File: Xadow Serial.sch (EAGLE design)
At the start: 29 parts, among them J1 CONNECTOR-HEADER-8P-3461050P1, J2 12p 0.5mm bottom contact, J3 12p 0.5mm bottom contact, J4 12p 0.5mm bottom contact, SW2 ADDR, U1 SC16IS750, U2 BSS138PS, X1 CTS_32X25_SMD

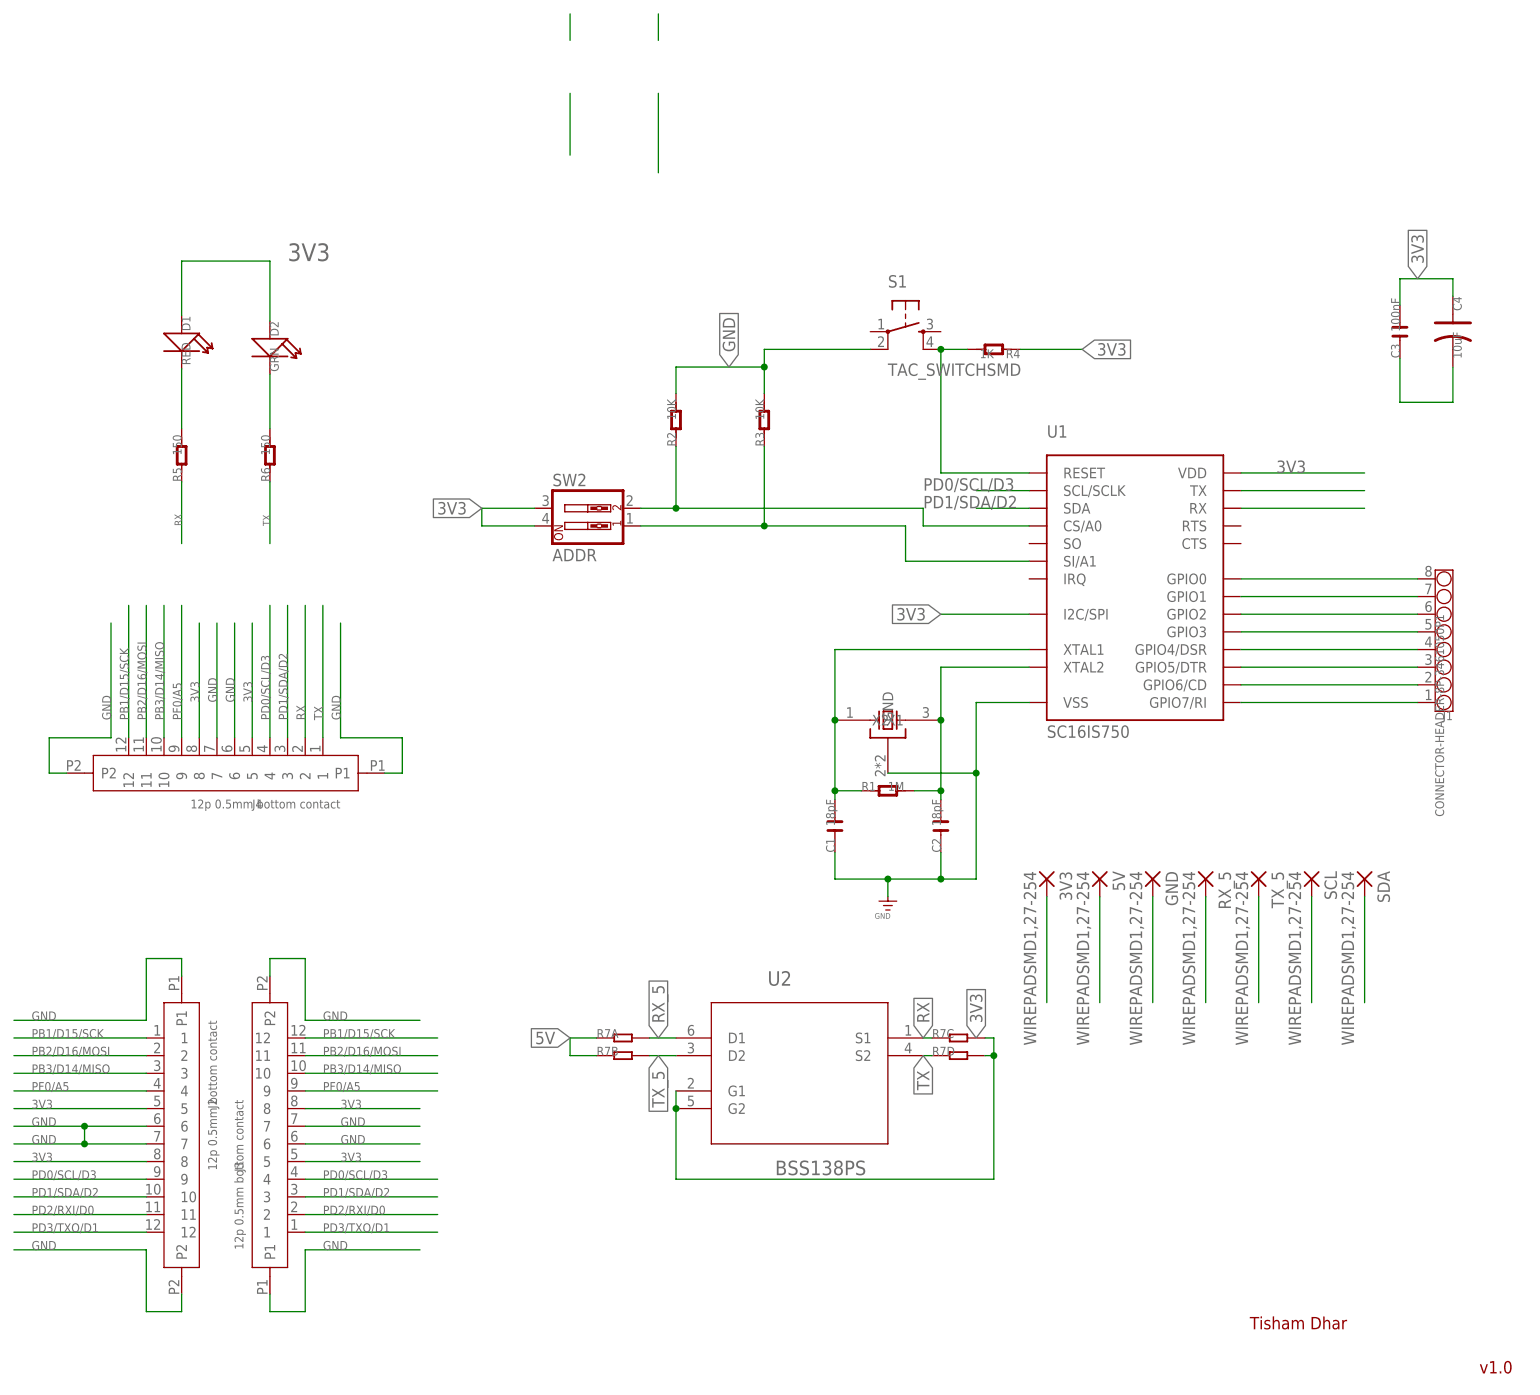
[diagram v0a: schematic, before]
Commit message: Fully routed with solder jumpers
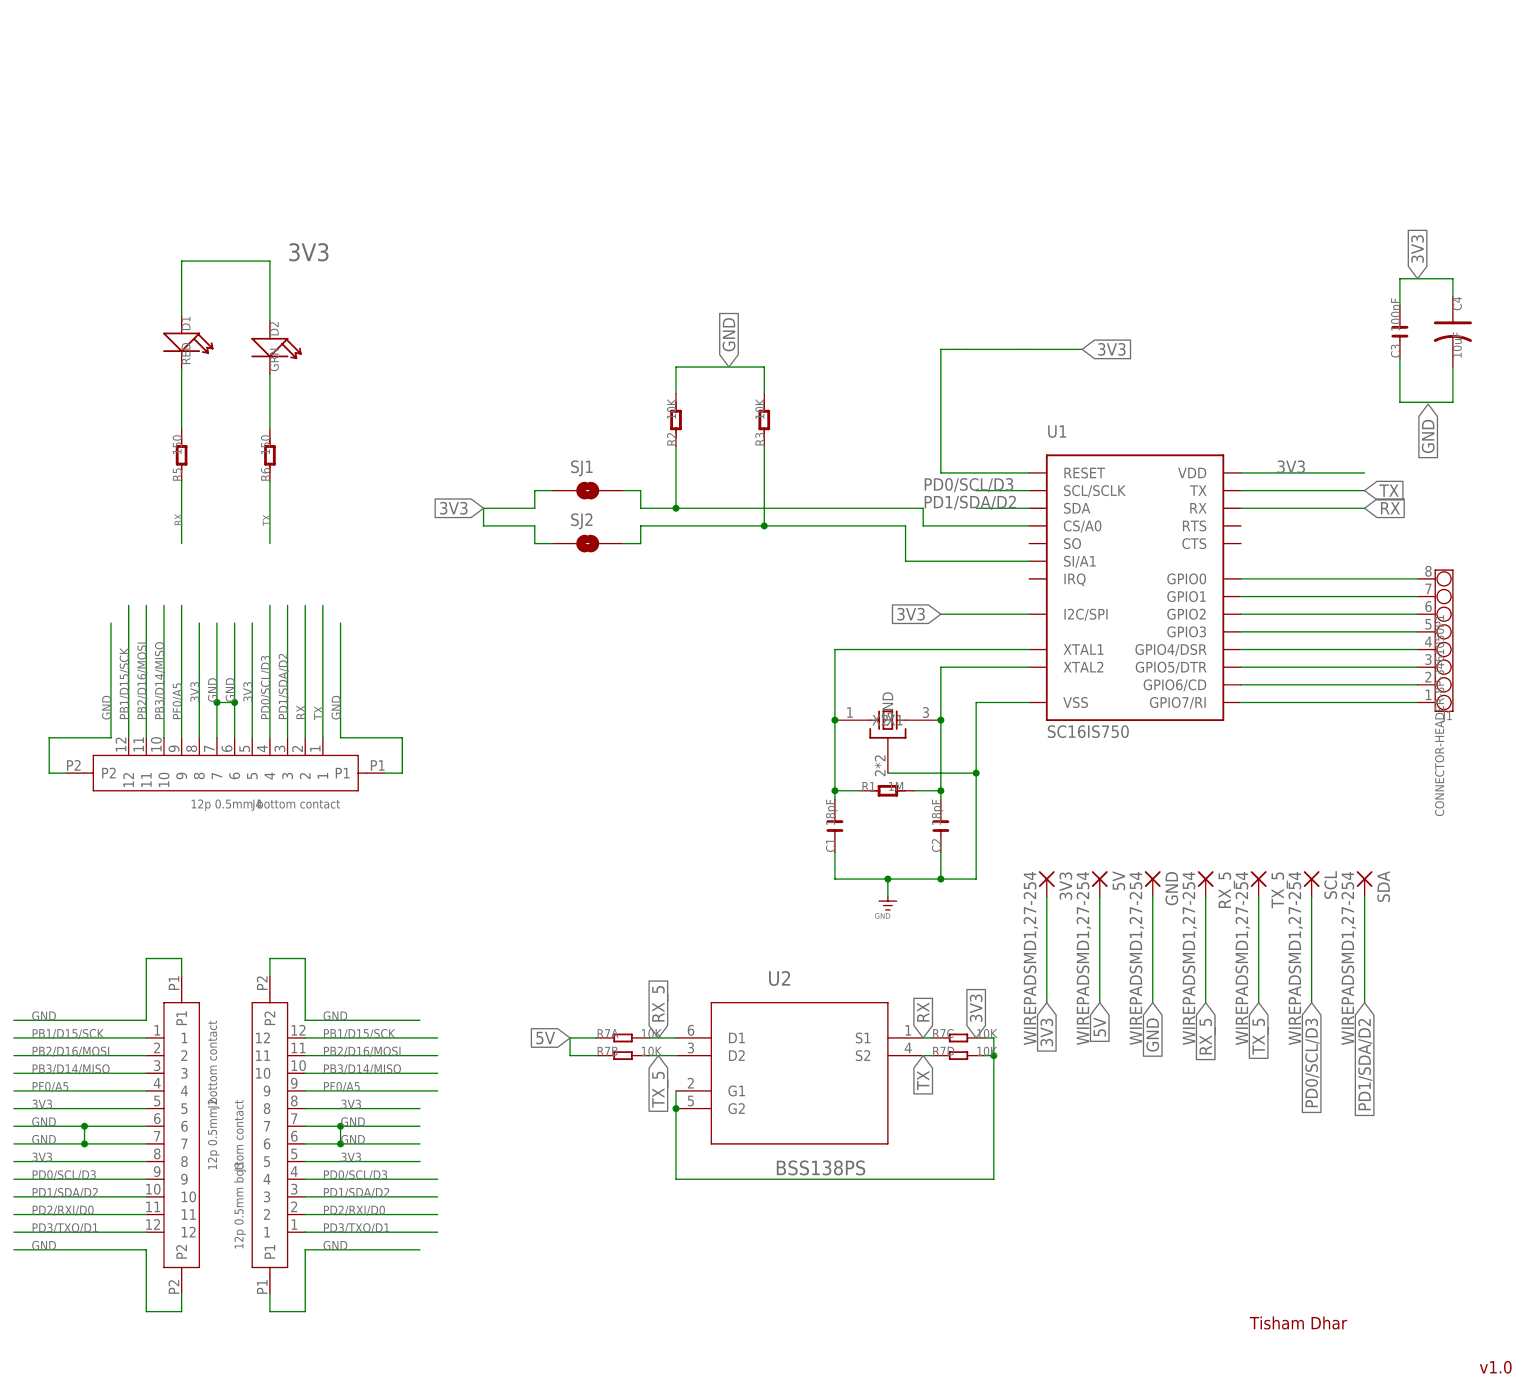
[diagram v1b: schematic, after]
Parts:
- removed R4: 1K, OPL:R-0603
- removed S1: TAC_SWITCHSMD, SparkFun-Electromechanical:TAC_SWITCHSMD
- removed SW2: ADDR, SparkFun-Electromechanical:SW_DIP-2-SMT-HALFSIZE
- added SJ1, SJ2: JUMPER-PAD-2-NO, SparkFun-Passives:JUMPER-PAD-2-NO
- R7: value (none) -> 10K
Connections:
- removed net N$17: C3.1, C4.2
- removed net N$5: R4.2, S1.4, U1.RESET
- net 3V3: now also SJ1.1, SJ2.1, U1.RESET; no longer R4.1, SW2.3, SW2.4
- net GND: now also C3.1, C4.2; no longer S1.2
- net N$3: now also SJ2.2; no longer SW2.1
- net N$4: now also SJ1.2; no longer SW2.2

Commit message: Fixed up labels
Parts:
- renumbered SJ1 to A0, SJ2 to A1
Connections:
- net N$11 renamed IO4
- net N$12 renamed IO5
- net N$13 renamed IO6
- net N$14 renamed IO7
- net N$6 renamed IO0
- net N$7 renamed IO1
- net N$8 renamed IO2
- net N$9 renamed IO3
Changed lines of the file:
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@@
 <part name="SDA" library="wirepad" deviceset="WIREPAD" device="SMD1,27-254"/>
 <part name="3V3" library="wirepad" deviceset="WIREPAD" device="SMD1,27-254"/>
-<part name="SJ1" library="SparkFun-Passives" deviceset="JUMPER-PAD-2-NO" device=""/>
-<part name="SJ2" library="SparkFun-Passives" deviceset="JUMPER-PAD-2-NO" device=""/>
+<part name="A0" library="SparkFun-Passives" deviceset="JUMPER-PAD-2-NO" device=""/>
+<part name="A1" library="SparkFun-Passives" deviceset="JUMPER-PAD-2-NO" device=""/>
 </parts>
 <sheets>
@@
 <instance part="SDA" gate="G$1" x="208.28" y="76.2" rot="R270"/>
 <instance part="3V3" gate="G$1" x="162.56" y="76.2" rot="R270"/>
-<instance part="SJ1" gate="G$1" x="96.52" y="132.08" smashed="yes">
+<instance part="A0" gate="G$1" x="96.52" y="132.08" smashed="yes">
 <attribute name="NAME" x="93.98" y="134.62" size="1.778" layer="95"/>
 </instance>
-<instance part="SJ2" gate="G$1" x="96.52" y="124.46" smashed="yes">
+<instance part="A1" gate="G$1" x="96.52" y="124.46" smashed="yes">
 <attribute name="NAME" x="93.98" y="127" size="1.778" layer="95"/>
 </instance>
@@
 <label x="81.534" y="129.54" size="1.778" layer="95" rot="R180" xref="yes"/>
 <wire x1="88.9" y1="129.54" x2="88.9" y2="132.08" width="0.1524" layer="91"/>
-<pinref part="SJ1" gate="G$1" pin="1"/>
+<pinref part="A0" gate="G$1" pin="1"/>
 <wire x1="88.9" y1="132.08" x2="91.44" y2="132.08" width="0.1524" layer="91"/>
 <wire x1="88.9" y1="127" x2="88.9" y2="124.46" width="0.1524" layer="91"/>
-<pinref part="SJ2" gate="G$1" pin="1"/>
+<pinref part="A1" gate="G$1" pin="1"/>
 <wire x1="88.9" y1="124.46" x2="91.44" y2="124.46" width="0.1524" layer="91"/>
 </segment>
@@
 <wire x1="121.92" y1="138.43" x2="121.92" y2="127" width="0.1524" layer="91"/>
 <wire x1="104.14" y1="127" x2="104.14" y2="124.46" width="0.1524" layer="91"/>
-<pinref part="SJ2" gate="G$1" pin="2"/>
+<pinref part="A1" gate="G$1" pin="2"/>
 <wire x1="104.14" y1="124.46" x2="101.6" y2="124.46" width="0.1524" layer="91"/>
 </segment>
@@
 <wire x1="109.22" y1="138.43" x2="109.22" y2="129.54" width="0.1524" layer="91"/>
 <pinref part="R2" gate="R" pin="1"/>
-<pinref part="SJ1" gate="G$1" pin="2"/>
+<pinref part="A0" gate="G$1" pin="2"/>
 <wire x1="101.6" y1="132.08" x2="104.14" y2="132.08" width="0.1524" layer="91"/>
 <wire x1="104.14" y1="132.08" x2="104.14" y2="129.54" width="0.1524" layer="91"/>
 </segment>
 </net>
-<net name="N$6" class="0">
+<net name="IO0" class="0">
 <segment>
 <pinref part="U1" gate="G$1" pin="GPIO0"/>
 <wire x1="190.5" y1="119.38" x2="215.9" y2="119.38" width="0.1524" layer="91"/>
 <pinref part="J1" gate="J" pin="8"/>
-</segment>
-</net>
-<net name="N$7" class="0">
+<label x="198.12" y="119.38" size="1.778" layer="95"/>
+</segment>
+</net>
+<net name="IO1" class="0">
 <segment>
 <pinref part="U1" gate="G$1" pin="GPIO1"/>
 <pinref part="J1" gate="J" pin="7"/>
 <wire x1="190.5" y1="116.84" x2="215.9" y2="116.84" width="0.1524" layer="91"/>
-</segment>
-</net>
-<net name="N$8" class="0">
+<label x="198.12" y="116.84" size="1.778" layer="95"/>
+</segment>
+</net>
+<net name="IO2" class="0">
 <segment>
 <pinref part="U1" gate="G$1" pin="GPIO2"/>
 <pinref part="J1" gate="J" pin="6"/>
 <wire x1="190.5" y1="114.3" x2="215.9" y2="114.3" width="0.1524" layer="91"/>
-</segment>
-</net>
-<net name="N$9" class="0">
+<label x="198.12" y="114.3" size="1.778" layer="95"/>
+</segment>
+</net>
+<net name="IO3" class="0">
 <segment>
 <pinref part="J1" gate="J" pin="5"/>
 <pinref part="U1" gate="G$1" pin="GPIO3"/>
 <wire x1="215.9" y1="111.76" x2="190.5" y2="111.76" width="0.1524" layer="91"/>
-</segment>
-</net>
-<net name="N$11" class="0">
+<label x="198.12" y="111.76" size="1.778" layer="95"/>
+</segment>
+</net>
+<net name="IO4" class="0">
 <segment>
 <pinref part="U1" gate="G$1" pin="GPIO4/DSR"/>
 <pinref part="J1" gate="J" pin="4"/>
 <wire x1="190.5" y1="109.22" x2="215.9" y2="109.22" width="0.1524" layer="91"/>
-</segment>
-</net>
-<net name="N$12" class="0">
+<label x="198.12" y="109.22" size="1.778" layer="95"/>
+</segment>
+</net>
+<net name="IO5" class="0">
 <segment>
 <pinref part="J1" gate="J" pin="3"/>
 <pinref part="U1" gate="G$1" pin="GPIO5/DTR"/>
 <wire x1="215.9" y1="106.68" x2="190.5" y2="106.68" width="0.1524" layer="91"/>
-</segment>
-</net>
-<net name="N$13" class="0">
+<label x="198.12" y="106.68" size="1.778" layer="95"/>
+</segment>
+</net>
+<net name="IO6" class="0">
 <segment>
 <pinref part="J1" gate="J" pin="2"/>
 <pinref part="U1" gate="G$1" pin="GPIO6/CD"/>
 <wire x1="215.9" y1="104.14" x2="190.5" y2="104.14" width="0.1524" layer="91"/>
-</segment>
-</net>
-<net name="N$14" class="0">
+<label x="198.12" y="104.14" size="1.778" layer="95"/>
+</segment>
+</net>
+<net name="IO7" class="0">
 <segment>
 <pinref part="J1" gate="J" pin="1"/>

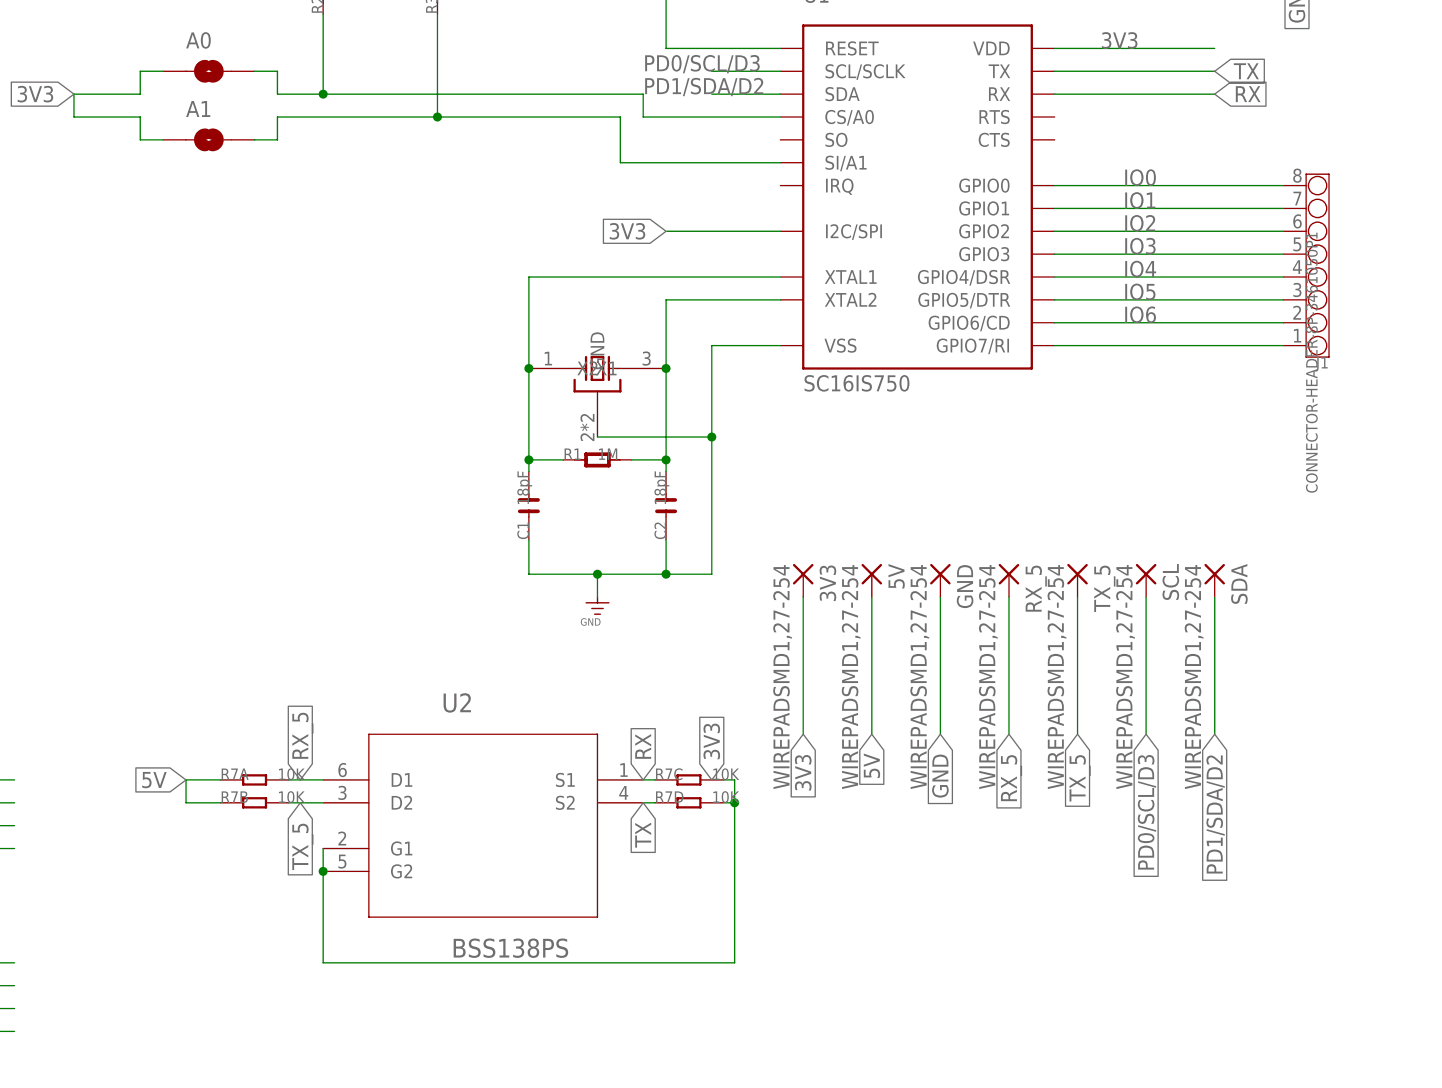
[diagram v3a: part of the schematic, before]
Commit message: Better crystal location
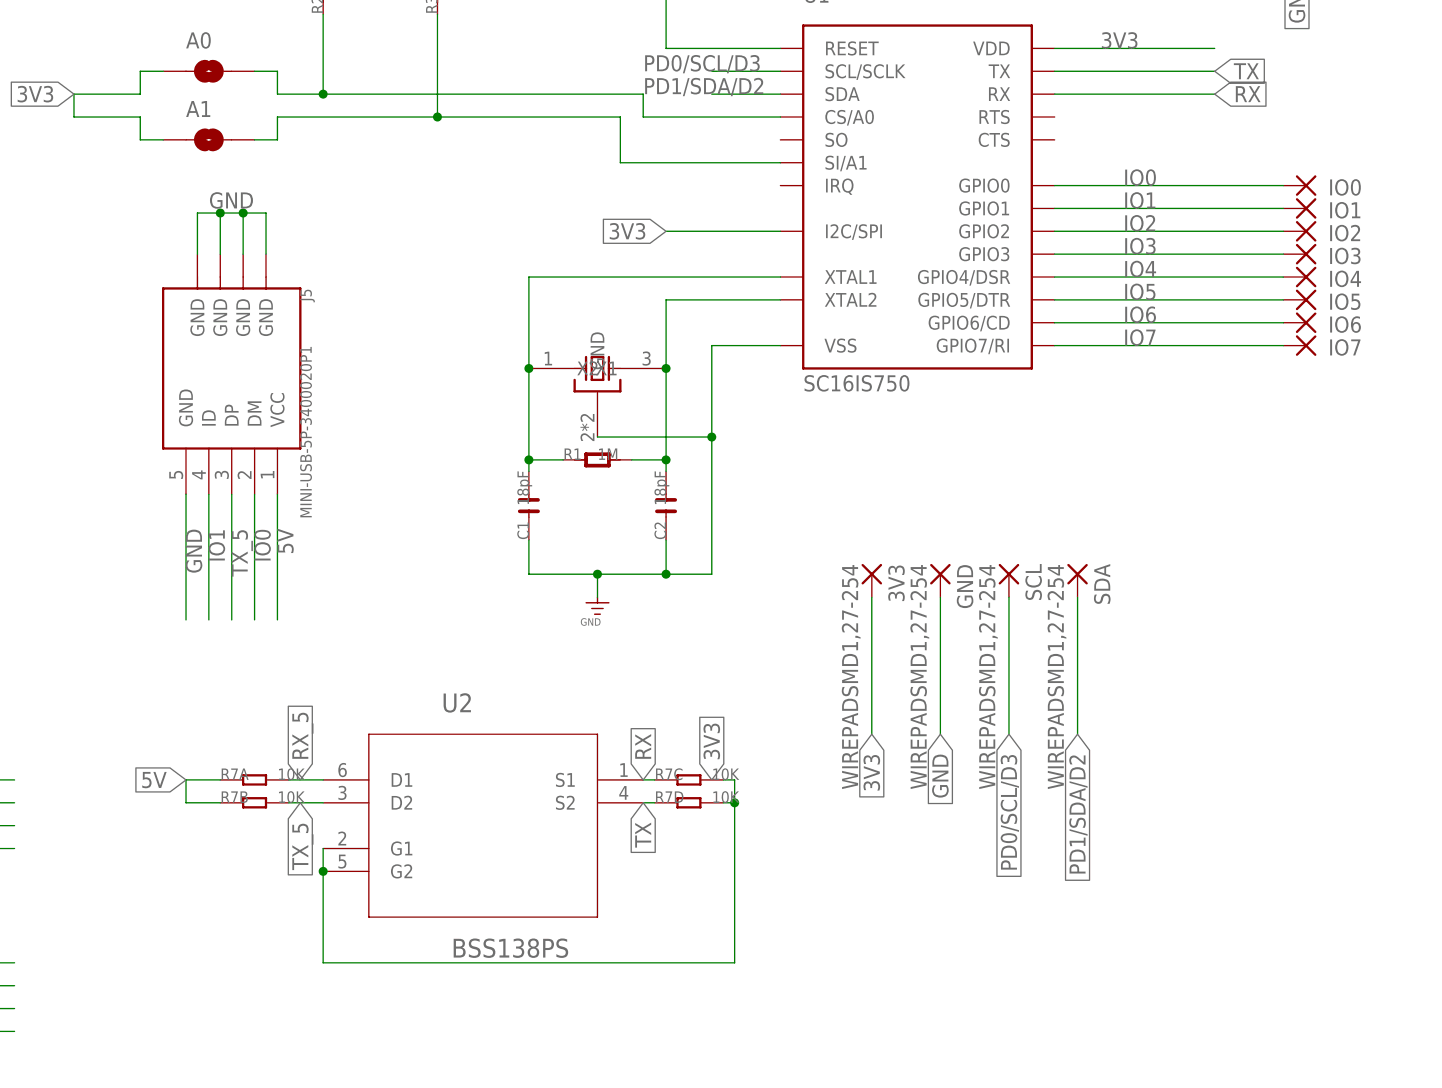
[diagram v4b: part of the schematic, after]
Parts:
- removed 5V, RX_5, TX_5: WIREPADSMD1,27-254, wirepad:WIREPADSMD1,27-254
- removed J1: CONNECTOR-HEADER-8P-3461050P1, OPL:CONNECTOR-HEADER-8P-3461050P1
- added IO0, IO1, IO2, IO3, IO4, IO5, IO6, IO7: WIREPADSMD1,27-254, wirepad:WIREPADSMD1,27-254
- added J5: MINI-USB-5P-3400020P1, Connector:MINI-USB-5P-3400020P1
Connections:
- net 5V: now also J5.VCC; no longer 5V.P
- net GND: now also J5.GND@1, J5.GND@2, J5.GND@3, J5.GND@4, J5.GND@5
- net IO0: now also IO0.P, J5.DM; no longer J1.8
- net IO1: now also IO1.P, J5.ID; no longer J1.7
- net IO2: now also IO2.P; no longer J1.6
- net IO3: now also IO3.P; no longer J1.5
- net IO4: now also IO4.P; no longer J1.4
- net IO5: now also IO5.P; no longer J1.3
- net IO6: now also IO6.P; no longer J1.2
- net IO7: now also IO7.P; no longer J1.1
- net RX_5: no longer RX_5.P
- net TX_5: now also J5.DP; no longer TX_5.P
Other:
- moved on the sheet: 3V3, SCL, SDA
